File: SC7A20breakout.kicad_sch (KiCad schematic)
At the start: 17 parts, among them J1 Qwiic_I2C_connector, J2 Qwiic_I2C_connector, J3 Conn_01x04, J4 Conn_01x04, U1 SC7A20

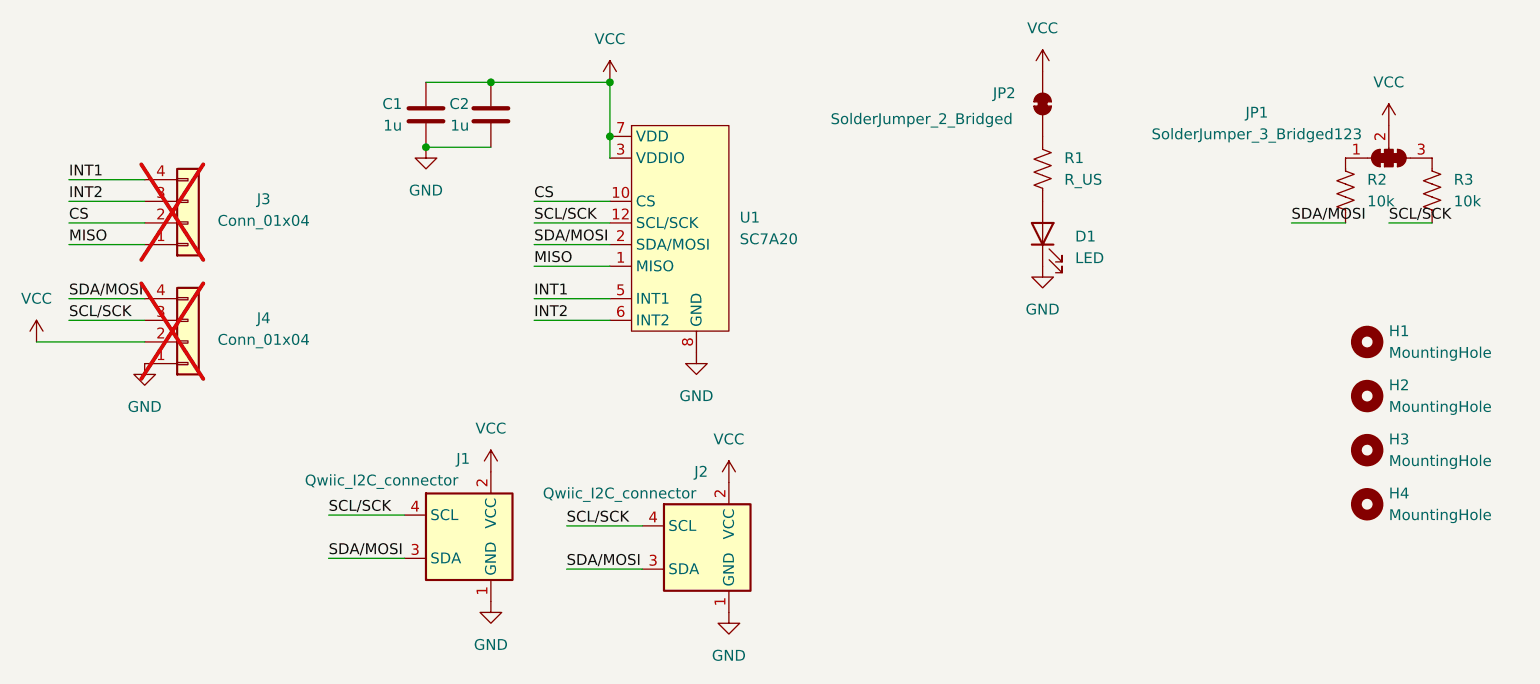
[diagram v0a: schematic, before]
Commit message: Correct hole spacing and labeling
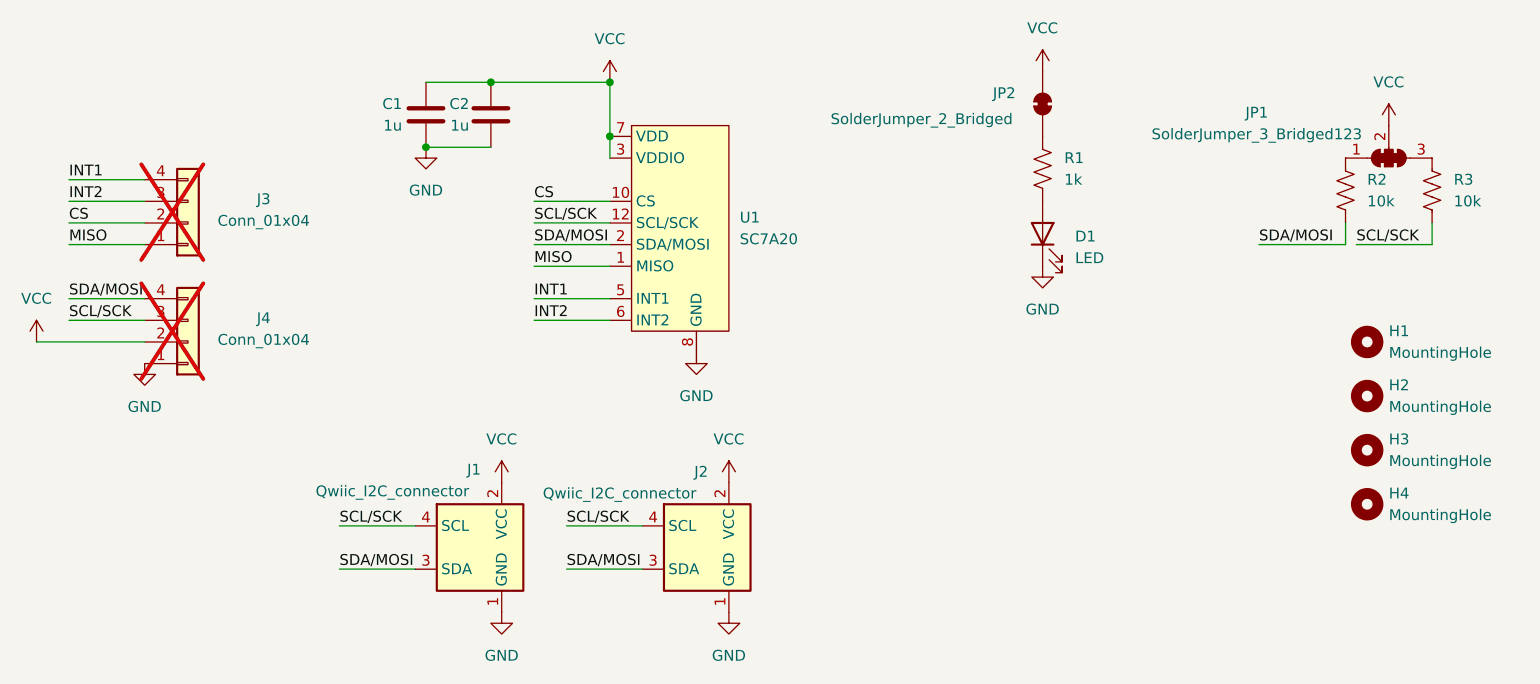
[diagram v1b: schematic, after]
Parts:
- C1, C2: LCSC (none) -> C1592
- D1: LCSC (none) -> C965799
- H1, H2, H3, H4: footprint MountingHole:MountingHole_4.3mm_M4 -> MountingHole:MountingHole_3.2mm_M3
- J1, J2: LCSC (none) -> C7430446
- R1: value R_US -> 1k; LCSC (none) -> C25585
- R2, R3: LCSC (none) -> C25804
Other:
- moved on the sheet: J1
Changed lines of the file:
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@@
 	(wire
 		(pts
-			(xy 196.85 38.1) (xy 201.93 38.1)
+			(xy 193.04 40.64) (xy 201.93 40.64)
 		)
 		(stroke
@@
 	(wire
 		(pts
-			(xy 96.52 40.64) (xy 105.41 40.64)
+			(xy 191.77 40.64) (xy 191.77 38.1)
 		)
 		(stroke
@@
 	(wire
 		(pts
-			(xy 100.33 73.66) (xy 109.22 73.66)
+			(xy 201.93 40.64) (xy 201.93 38.1)
 		)
 		(stroke
@@
 	(wire
 		(pts
-			(xy 105.41 21.59) (xy 105.41 27.94)
+			(xy 96.52 40.64) (xy 105.41 40.64)
 		)
 		(stroke
@@
 	(wire
 		(pts
-			(xy 105.41 27.94) (xy 105.41 30.48)
+			(xy 100.33 73.66) (xy 109.22 73.66)
 		)
 		(stroke
@@
 	(wire
 		(pts
-			(xy 185.42 38.1) (xy 191.77 38.1)
+			(xy 105.41 21.59) (xy 105.41 27.94)
 		)
 		(stroke
@@
 	(wire
 		(pts
-			(xy 72.39 77.47) (xy 81.28 77.47)
+			(xy 105.41 27.94) (xy 105.41 30.48)
 		)
 		(stroke
@@
 	(wire
 		(pts
-			(xy 96.52 46.99) (xy 105.41 46.99)
+			(xy 181.61 40.64) (xy 191.77 40.64)
 		)
 		(stroke
@@
 	(wire
 		(pts
-			(xy 72.39 72.39) (xy 81.28 72.39)
+			(xy 73.66 78.74) (xy 82.55 78.74)
 		)
 		(stroke
@@
 	(wire
 		(pts
-			(xy 41.91 49.53) (xy 50.8 49.53)
+			(xy 96.52 46.99) (xy 105.41 46.99)
 		)
 		(stroke
@@
 	(wire
 		(pts
-			(xy 41.91 40.64) (xy 50.8 40.64)
+			(xy 73.66 73.66) (xy 82.55 73.66)
 		)
 		(stroke
@@
 	(wire
 		(pts
-			(xy 96.52 43.18) (xy 105.41 43.18)
+			(xy 41.91 49.53) (xy 50.8 49.53)
 		)
 		(stroke
@@
 	(wire
 		(pts
-			(xy 41.91 46.99) (xy 50.8 46.99)
+			(xy 41.91 40.64) (xy 50.8 40.64)
 		)
 		(stroke
@@
 		)
 	)
+	(wire
+		(pts
+			(xy 96.52 43.18) (xy 105.41 43.18)
+		)
+		(stroke
+			(width 0)
+			(type default)
+		)
+	)
+	(wire
+		(pts
+			(xy 41.91 46.99) (xy 50.8 46.99)
+		)
+		(stroke
+			(width 0)
+			(type default)
+		)
+	)
 	(label "INT2"
 		(at 41.91 35.56 0)
@@
 	)
 	(label "SCL{slash}SCK"
-		(at 72.39 72.39 0)
+		(at 73.66 73.66 0)
 		(fields_autoplaced yes)
 		(effects
@@
 	)
 	(label "SDA{slash}MOSI"
-		(at 72.39 77.47 0)
+		(at 73.66 78.74 0)
 		(fields_autoplaced yes)
 		(effects
@@
 	)
 	(label "SDA{slash}MOSI"
-		(at 185.42 38.1 0)
+		(at 181.61 40.64 0)
 		(fields_autoplaced yes)
 		(effects
@@
 	)
 	(label "SCL{slash}SCK"
-		(at 196.85 38.1 0)
+		(at 193.04 40.64 0)
 		(fields_autoplaced yes)
 		(effects
@@
 			)
 		)
+		(property "LCSC" "C25804"
+			(at 201.93 34.29 0)
+			(effects
+				(font
+					(size 1.27 1.27)
+				)
+				(hide yes)
+			)
+		)
 		(pin "1"
 		)
@@
 			)
 		)
+		(property "LCSC" "C25804"
+			(at 191.77 34.29 0)
+			(effects
+				(font
+					(size 1.27 1.27)
+				)
+				(hide yes)
+			)
+		)
 		(pin "1"
 		)
@@
 			)
 		)
-		(property "Footprint" "MountingHole:MountingHole_4.3mm_M4"
+		(property "Footprint" "MountingHole:MountingHole_3.2mm_M3"
 			(at 194.31 64.77 0)
 			(effects
@@
 			)
 		)
+		(property "LCSC" "C1592"
+			(at 91.44 25.4 0)
+			(effects
+				(font
+					(size 1.27 1.27)
+				)
+				(hide yes)
+			)
+		)
 		(pin "2"
 		)
@@
 			)
 		)
+		(property "LCSC" "C7430446"
+			(at 116.84 76.2 0)
+			(effects
+				(font
+					(size 1.27 1.27)
+				)
+				(hide yes)
+			)
+		)
 		(pin "MP"
 		)
@@
 	(symbol
 		(lib_id "power:VCC")
-		(at 91.44 67.31 0)
+		(at 92.71 68.58 0)
 		(unit 1)
 		(exclude_from_sim no)
@@
 		(fields_autoplaced yes)
 		(property "Reference" "#PWR06"
-			(at 91.44 71.12 0)
+			(at 92.71 72.39 0)
 			(effects
 				(font
@@
 		)
 		(property "Value" "VCC"
-			(at 91.44 62.23 0)
+			(at 92.71 63.5 0)
 			(effects
 				(font
@@
 		)
 		(property "Footprint" ""
-			(at 91.44 67.31 0)
+			(at 92.71 68.58 0)
 			(effects
 				(font
@@
 		)
 		(property "Datasheet" ""
-			(at 91.44 67.31 0)
+			(at 92.71 68.58 0)
 			(effects
 				(font
@@
 		)
 		(property "Description" "Power symbol creates a global label with name \"VCC\""
-			(at 91.44 67.31 0)
+			(at 92.71 68.58 0)
 			(effects
 				(font
@@
 			)
 		)
+		(property "LCSC" "C1592"
+			(at 83.82 25.4 0)
+			(effects
+				(font
+					(size 1.27 1.27)
+				)
+				(hide yes)
+			)
+		)
 		(pin "2"
 		)
@@
 	(symbol
 		(lib_id "maxkicad:Qwiic_I2C")
-		(at 88.9 74.93 0)
+		(at 90.17 76.2 0)
 		(unit 1)
 		(exclude_from_sim no)
@@
 		(dnp no)
 		(property "Reference" "J1"
-			(at 87.376 65.786 0)
+			(at 88.646 67.056 0)
 			(effects
 				(font
@@
 		)
 		(property "Value" "Qwiic_I2C_connector"
-			(at 69.596 68.326 0)
+			(at 70.866 69.596 0)
 			(effects
 				(font
@@
 		)
 		(property "Footprint" "Connector_JST:JST_SH_SM04B-SRSS-TB_1x04-1MP_P1.00mm_Horizontal"
-			(at 92.71 81.28 0)
+			(at 93.98 82.55 0)
 			(effects
 				(font
@@
 		)
 		(property "Datasheet" ""
-			(at 92.71 83.82 0)
+			(at 93.98 85.09 0)
 			(effects
 				(font
@@
 		)
 		(property "Description" ""
-			(at 88.9 74.93 0)
+			(at 90.17 76.2 0)
+			(effects
+				(font
+					(size 1.27 1.27)
+				)
+				(hide yes)
+			)
+		)
+		(property "LCSC" "C7430446"
+			(at 90.17 76.2 0)
 			(effects
 				(font
@@
 			)
 		)
-		(property "Footprint" "MountingHole:MountingHole_4.3mm_M4"
+		(property "Footprint" "MountingHole:MountingHole_3.2mm_M3"
 			(at 194.31 58.42 0)
 			(effects
@@
 			)
 		)
-		(property "Value" "R_US"
+		(property "Value" "1k"
 			(at 158.75 33.0199 0)
 			(effects
@@
 			)
 		)
+		(property "LCSC" "C25585"
+			(at 156.21 31.75 0)
+			(effects
+				(font
+					(size 1.27 1.27)
+				)
+				(hide yes)
+			)
+		)
 		(pin "1"
 		)
@@
 			)
 		)
-		(property "Footprint" "MountingHole:MountingHole_4.3mm_M4"
+		(property "Footprint" "MountingHole:MountingHole_3.2mm_M3"
 			(at 194.31 71.12 0)
 			(effects
@@
 			)
 		)
-		(property "Footprint" "MountingHole:MountingHole_4.3mm_M4"
+		(property "Footprint" "MountingHole:MountingHole_3.2mm_M3"
 			(at 194.31 52.07 0)
 			(effects
@@
 	(symbol
 		(lib_id "power:GND")
-		(at 91.44 82.55 0)
+		(at 92.71 83.82 0)
 		(unit 1)
 		(exclude_from_sim no)
@@
 		(fields_autoplaced yes)
 		(property "Reference" "#PWR02"
-			(at 91.44 88.9 0)
+			(at 92.71 90.17 0)
 			(effects
 				(font
@@
 		)
 		(property "Value" "GND"
-			(at 91.44 87.63 0)
+			(at 92.71 88.9 0)
 			(effects
 				(font
@@
 		)
 		(property "Footprint" ""
-			(at 91.44 82.55 0)
+			(at 92.71 83.82 0)
 			(effects
 				(font
@@
 		)
 		(property "Datasheet" ""
-			(at 91.44 82.55 0)
+			(at 92.71 83.82 0)
 			(effects
 				(font
@@
 		)
 		(property "Description" "Power symbol creates a global label with name \"GND\" , ground"
-			(at 91.44 82.55 0)
+			(at 92.71 83.82 0)
 			(effects
 				(font
@@
 			(at 156.21 39.37 0)
 			(effects
+				(font
+					(size 1.27 1.27)
+				)
+				(hide yes)
+			)
+		)
+		(property "LCSC" "C965799"
+			(at 156.21 39.37 0)
+			(effects

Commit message: Switched to JLCPCB basic assembly parts
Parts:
- C1, C2: LCSC C1592 -> C15849
- D1: LCSC C965799 -> C2286
- R1: LCSC C25585 -> C21190
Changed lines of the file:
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@@
 			)
 		)
-		(property "LCSC" "C1592"
+		(property "LCSC" " C15849"
 			(at 91.44 25.4 0)
 			(effects
@@
 			)
 		)
-		(property "LCSC" "C1592"
+		(property "LCSC" " C15849"
 			(at 83.82 25.4 0)
 			(effects
@@
 			)
 		)
-		(property "LCSC" "C25585"
+		(property "LCSC" "C21190"
 			(at 156.21 31.75 0)
 			(effects
@@
 			)
 		)
-		(property "LCSC" "C965799"
+		(property "LCSC" " C2286"
 			(at 156.21 39.37 0)
 			(effects
